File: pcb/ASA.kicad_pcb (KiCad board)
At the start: 2 copper layers, 54.1 x 30.5 mm, 35 parts, among them J1 Screw_Terminal_01x02, J2 Conn_01x03_Pin, Q1 AO3400A, U1 LM386

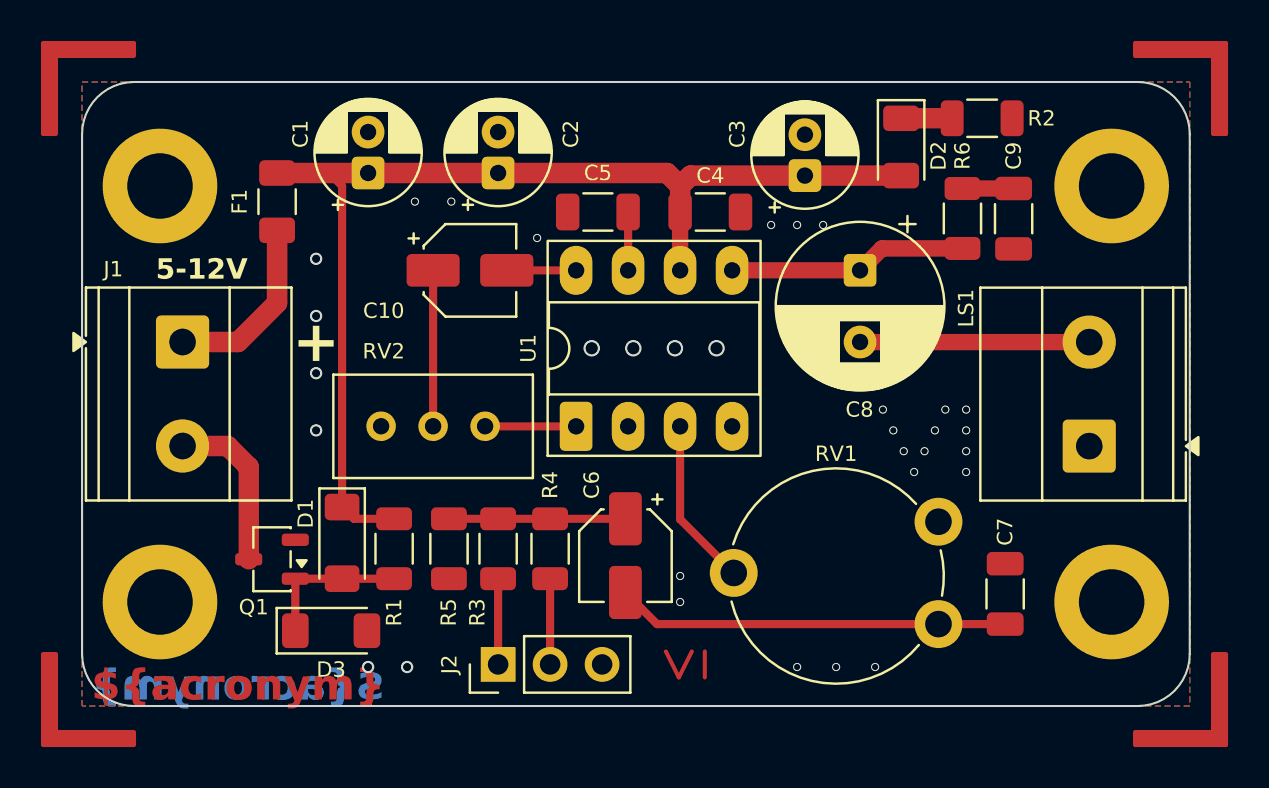
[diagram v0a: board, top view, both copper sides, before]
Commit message: Add bass boost option
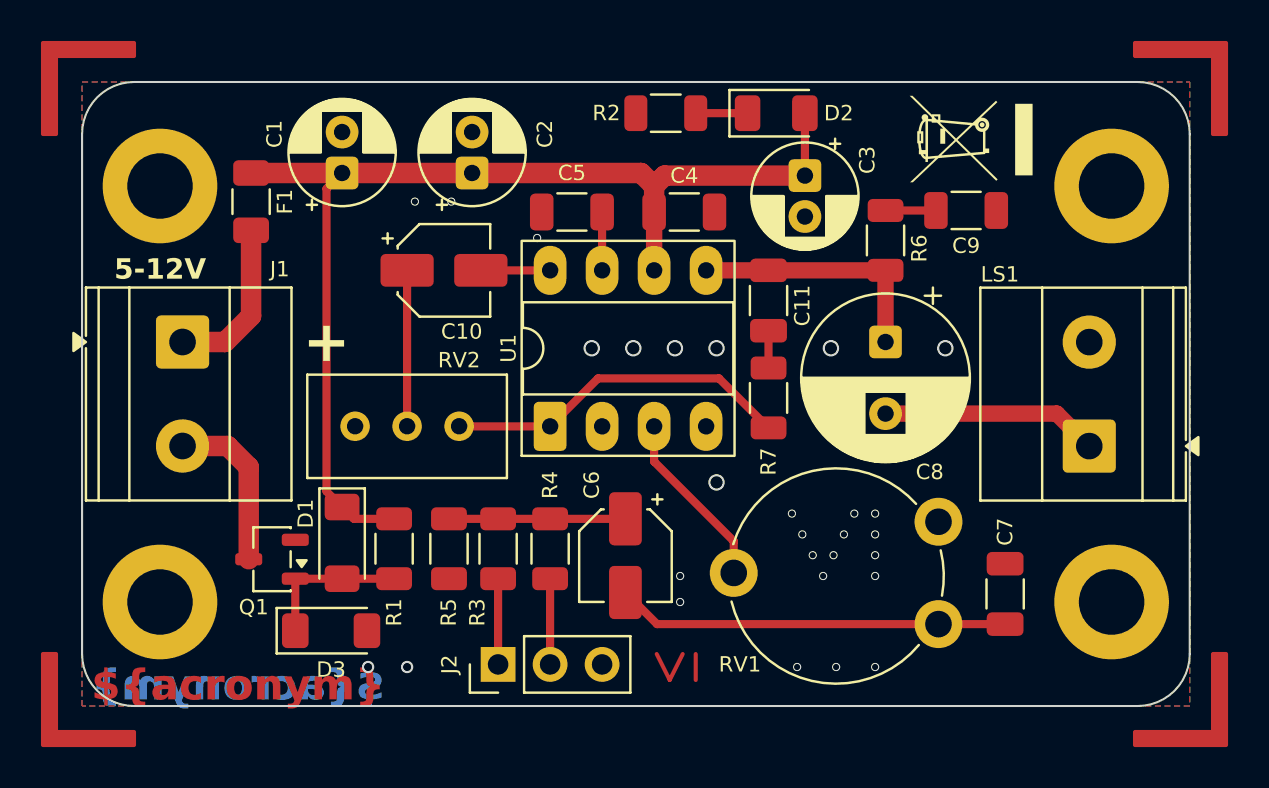
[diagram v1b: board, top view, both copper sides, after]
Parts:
- added C11: n.B., Capacitor_SMD:C_1206_3216Metric, F.Cu at (156.7, 81.8)
- added R7: n.B., Resistor_SMD:R_1206_3216Metric, F.Cu at (156.7, 86.6)
- FID2: moved to F.Cu
- moved FID2 20.1 mm to (166.6, 73.9), turned to 90 degrees
- moved R2 15.5 mm to (151.7, 72.6), turned to 180 degrees
- moved D2 6.32 mm to (157.1, 72.6), turned to 0 degrees
- moved R6 3.91 mm to (162.4, 78.9)
- moved C8 3.71 mm to (162.4, 83.8)
- moved C9 2.35 mm to (166.4, 77.4), turned to 0 degrees
- moved F1 1.27 mm to (131.4, 77.0)
- moved C1 1.27 mm to (135.9, 75.6)
- moved C10 1.27 mm to (140.9, 80.3)
- moved C2 1.27 mm to (142.2, 75.6)
- moved C4 1.27 mm to (152.6, 77.5)
- moved C5 1.27 mm to (147.1, 77.5)
- moved RV2 1.27 mm to (141.6, 87.9)
- moved U1 1.27 mm to (146.1, 87.9)
- turned C3 to -90 degrees
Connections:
- LS1 pad 1: GND -> Net-(C8-Pad2)
- LS1 pad 2: Net-(C8-Pad2) -> GND
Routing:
- net Net-(R7-Pad1): track 4.45 -> 17.1 mm
- net +5V: track 57.0 -> 58.9 mm
- net Net-(C11-Pad2): track 0.00 -> 1.82 mm
- net Net-(J1-Pin_1): track 8.96 -> 8.06 mm
- net Net-(C8-Pad2): track 11.2 -> 10.6 mm
- net Net-(C11-Pad1): track 11.7 -> 12.3 mm
- net Net-(U1-+): track 8.25 -> 8.77 mm
- net GND: vias 32 -> 28
